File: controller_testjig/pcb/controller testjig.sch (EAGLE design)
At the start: 46 parts, among them IC1 AD8041R, J1 POWER_JACKPTH, SW2 BUTTON_2

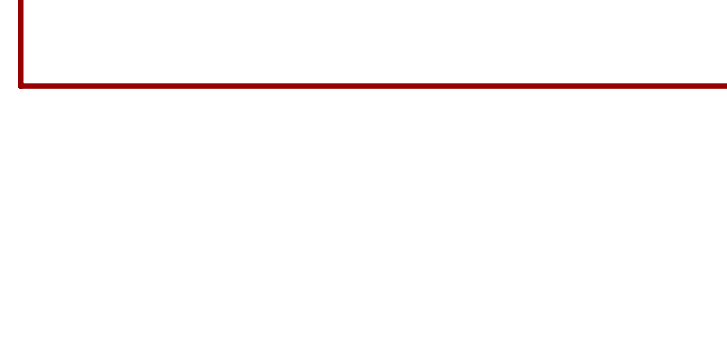
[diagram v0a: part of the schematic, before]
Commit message: Add notes for reworking controller testjig pcb
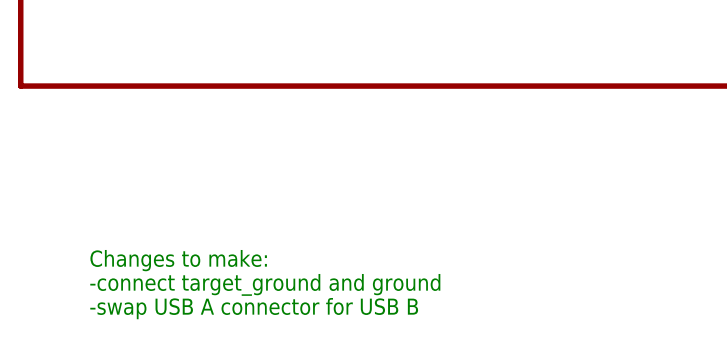
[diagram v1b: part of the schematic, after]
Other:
- note added: "Changes to make: -connect target_ground and ground -swap USB A connector for USB B"
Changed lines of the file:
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@@
 Cute hack to generate variable output voltage.
 Use a rail-to-rail opamp, &gt;30mA output.</text>
+<text x="-124.46" y="-162.56" size="1.778" layer="91">Changes to make:
+-connect target_ground and ground
+-swap USB A connector for USB B</text>
 </plain>
 <instances>

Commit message: Update production test to minimal working function
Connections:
- net TARGET_USB_D+: now also U$1.5, U$3.D+; no longer U$1.6, U$3.D-
- net TARGET_USB_D-: now also U$1.6, U$3.D-; no longer U$1.5, U$3.D+
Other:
- note added: "Changes to make: -connect target_ground and ground -swap USB A connector for USB B -target_pa4 connection causes the target to hang -Signal N$1 not connected on board, need to jump between R26 and R27"
- note removed: "Changes to make: -connect target_ground and ground -swap USB A connector for USB B"
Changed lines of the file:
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@@
 <text x="-124.46" y="-162.56" size="1.778" layer="91">Changes to make:
 -connect target_ground and ground
--swap USB A connector for USB B</text>
+-swap USB A connector for USB B
+-target_pa4 connection causes the target to hang
+-Signal N$1 not connected on board, need to jump between R26 and R27</text>
 </plain>
 <instances>
@@
 </segment>
 </net>
-<net name="TARGET_USB_D-" class="0">
+<net name="TARGET_USB_D+" class="0">
 <segment>
 <pinref part="U$1" gate="G$1" pin="5"/>
@@
 </segment>
 </net>
-<net name="TARGET_USB_D+" class="0">
+<net name="TARGET_USB_D-" class="0">
 <segment>
 <pinref part="U$1" gate="G$1" pin="6"/>
